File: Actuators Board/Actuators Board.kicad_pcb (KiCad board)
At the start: 2 copper layers, 96 parts, among them IC1 BD62120AEFJ-E2, J10 Conn_01x02_Male, J3 USB_C_Receptacle_USB2.0, J4 Conn_01x03_Male, J5 Conn_01x06_Male, J9 Conn_01x02_Male, Q1 MMDT2222A, Q2 SI2366DS, U1 ESP32-PICO-D4, U2 TPS54233D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

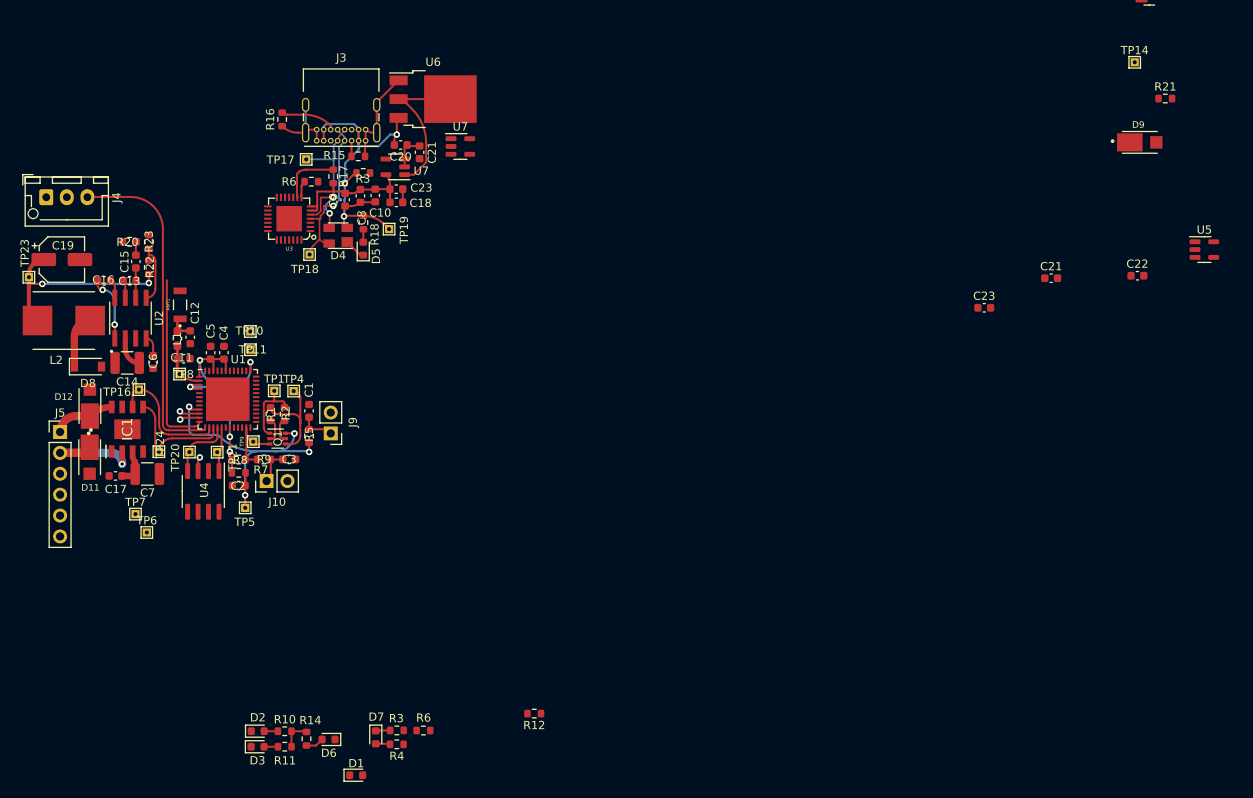
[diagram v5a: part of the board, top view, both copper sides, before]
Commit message: Swapped LDO to RT9025-25GSP & moved components closer together
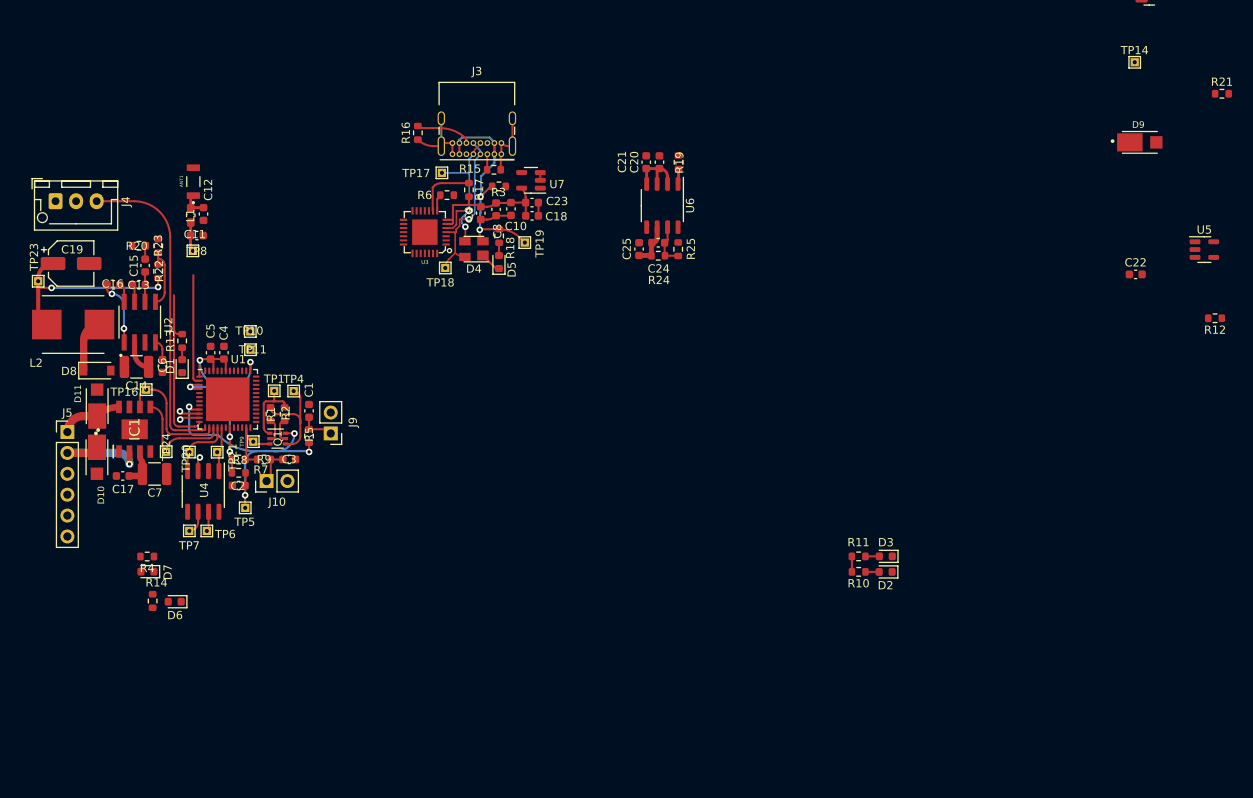
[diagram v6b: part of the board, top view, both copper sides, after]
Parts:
- removed the C21 at (260.5, 91.7)
- removed the C23 at (252.3, 95.3)
- removed the R3 at (180.9, 146.7)
- removed the R6 at (184.1, 146.7)
- removed the U7 at (188.6, 75.6)
- added C24: 0.1uF, Capacitor_SMD:C_0603_1608Metric, F.Cu at (212.7, 87.3)
- added C25: 10uF, Capacitor_SMD:C_0603_1608Metric, F.Cu at (210.4, 88.1)
- added R13: 470, Resistor_SMD:R_0603_1608Metric, F.Cu at (154.8, 99.3)
- added R19: 100k, Resistor_SMD:R_0603_1608Metric, F.Cu at (215.2, 77.6)
- added R24: 147k, Resistor_SMD:R_0603_1608Metric, F.Cu at (212.7, 88.9)
- added R25: 47k, Resistor_SMD:R_0603_1608Metric, F.Cu at (215.1, 88.1)
- C21: value 22uF -> 1uF
- U6: value AZ1084-3.3 -> RT9025-25GSP; footprint Package_TO_SOT_SMD:TO-252-3_TabPin2 -> Package_SO:SOP-8_3.9x4.9mm_P1.27mm
- moved R12 95.7 mm to (280.4, 96.5)
- moved D3 79.8 mm to (240.4, 125.5), turned to 180 degrees
- moved D2 78.8 mm to (240.3, 127.4), turned to 180 degrees
- moved R11 73.5 mm to (237.1, 125.5), turned to 0 degrees
- moved R10 72.5 mm to (237.1, 127.4), turned to 0 degrees
- moved D1 54.1 mm to (154.8, 102.4), turned to 90 degrees
- moved R4 38.0 mm to (150.5, 125.5)
- moved D7 34.3 mm to (150.6, 127.3), turned to 180 degrees
- moved C20 31.5 mm to (212.8, 77.5), turned to -90 degrees
- moved U6 30.7 mm to (213.2, 82.8), turned to -90 degrees
- moved C21 27.6 mm to (211.2, 77.5)
- moved D6 25.1 mm to (153.9, 131.0)
- moved R14 25.1 mm to (151.2, 130.9)
- moved C9 16.6 mm to (191.1, 83.8)
- moved D4 16.6 mm to (190.3, 88.1)
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- renumbered D11 to D10, D12 to D11
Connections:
- C21 pad 2: (no net) -> VBUS
- D1 pad 2: /SolEN -> Net-(D1-Pad2)
- R3 pad 2: (no net) -> Net-(R3-Pad2)
- U6 pad 1: GND -> Net-(R19-Pad1)
- U6 pad 2: Net-(C21-Pad2) -> VBUS
- U7 pad 1: Net-(C21-Pad2) -> Net-(U7-Pad1)
- U7 pad 4: (no net) -> unconnected-(U7-Pad4)
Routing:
- net Net-(C21-Pad2): track 18.6 -> 0.00 mm
- net /LNA_IN: track 6.27 -> 17.1 mm
- net GND: track 38.0 -> 29.2 mm
- net Net-(U7-Pad1): track 0.00 -> 5.39 mm
- net Net-(C24-Pad1): track 0.00 -> 5.32 mm
- net /CAN_LOW: track 0.00 -> 2.89 mm
- net /CAN_HIGH: track 0.00 -> 2.44 mm
- net Net-(D6-Pad2): track 2.20 -> 0.00 mm
- net Net-(R19-Pad1): track 0.00 -> 1.85 mm
- net /ServoPWM: track 40.7 -> 38.9 mm
- net Net-(D7-Pad2): track 1.76 -> 0.00 mm
- net +3V3: track 61.1 -> 59.3 mm
- net VBUS: track 38.2 -> 39.8 mm, vias 3 -> 2
- net Net-(D1-Pad2): track 0.00 -> 1.46 mm
- net /HBridgeDIR1: track 15.0 -> 14.1 mm
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
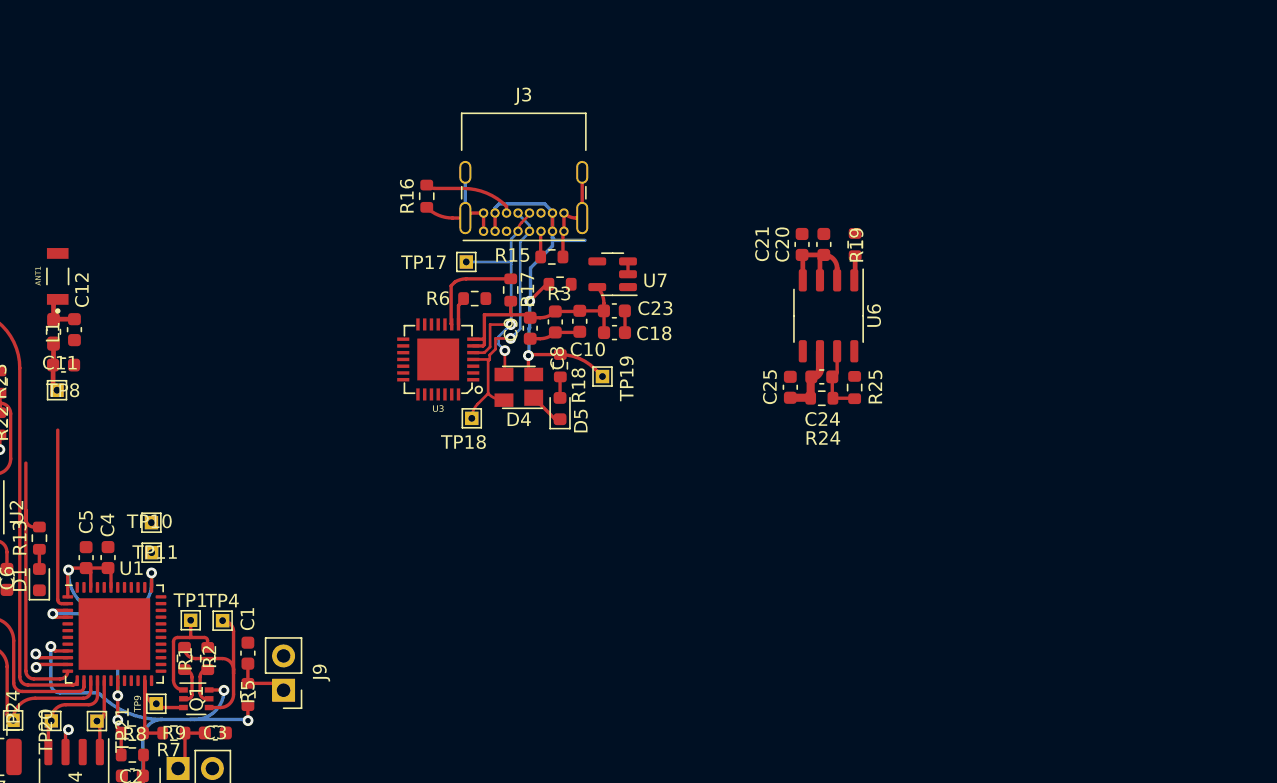
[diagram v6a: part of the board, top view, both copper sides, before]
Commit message: condensed usb layout
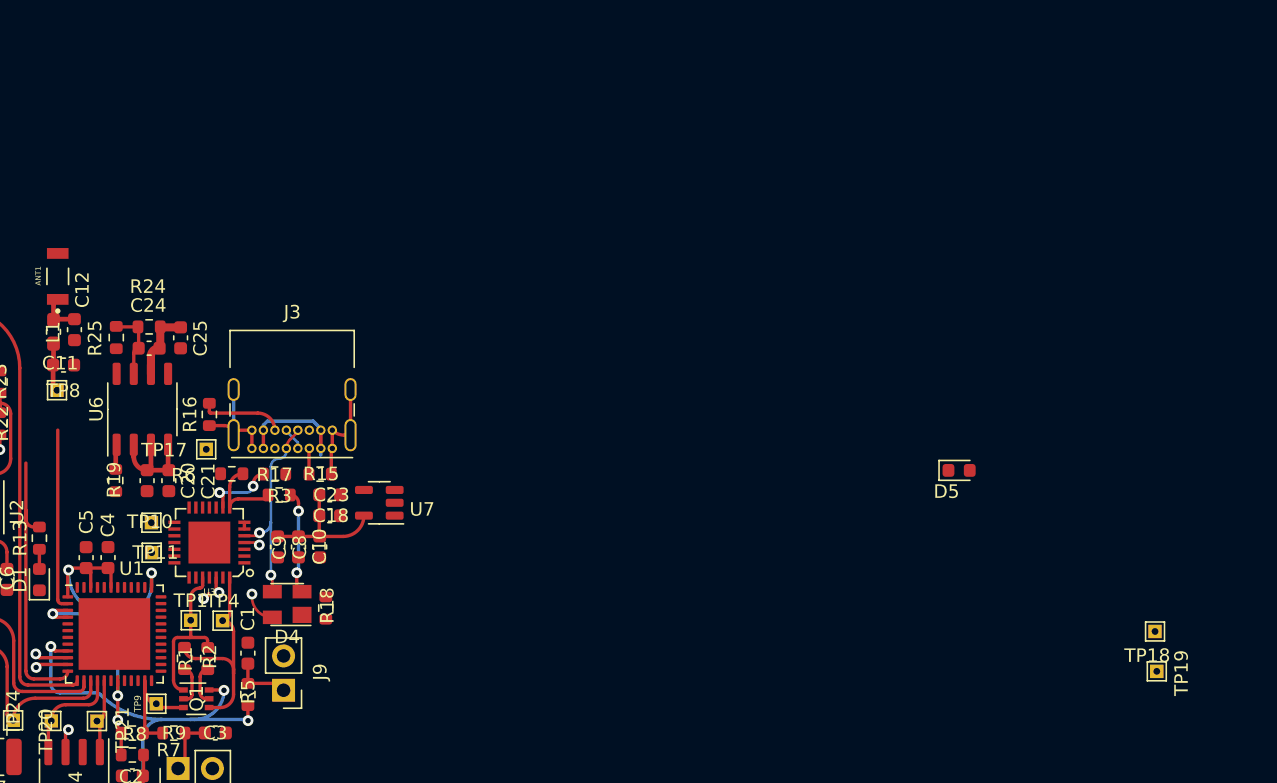
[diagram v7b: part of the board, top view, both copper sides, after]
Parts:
- moved R19 57.4 mm to (160.4, 95.0), turned to -90 degrees
- moved R25 54.8 mm to (160.5, 84.4), turned to -90 degrees
- moved C20 53.0 mm to (162.8, 95.0), turned to 90 degrees
- moved TP18 53.0 mm to (237.3, 106.2)
- moved U6 51.2 mm to (162.4, 89.8), turned to 90 degrees
- moved R24 50.1 mm to (162.9, 83.7), turned to 180 degrees
- moved C21 50.0 mm to (164.4, 95.0), turned to 90 degrees
- moved C24 49.8 mm to (162.9, 85.2), turned to 0 degrees
- moved TP19 46.5 mm to (237.5, 109.1)
- moved C25 45.3 mm to (165.2, 84.5), turned to 90 degrees
- moved D5 29.9 mm to (222.8, 94.3), turned to 0 degrees
- moved R3 26.0 mm to (172.5, 96.1), turned to 180 degrees
- moved C10 25.5 mm to (175.5, 99.9)
- moved C8 25.3 mm to (174.0, 99.9)
- moved C23 25.1 mm to (176.3, 96.1)
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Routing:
- net /USB -> UART/Data+: track 20.4 -> 5.50 mm
- net VBUS: track 39.8 -> 25.9 mm
- net GND: track 29.2 -> 19.3 mm
- net +3V3: track 59.3 -> 52.5 mm
- net /USB -> UART/Data-: track 21.0 -> 15.5 mm, vias 2 -> 1
- net Net-(R3-Pad2): track 1.73 -> 6.46 mm
- net /RTS: track 8.59 -> 12.2 mm
- net /DTR: track 13.0 -> 16.5 mm
- net Net-(R17-Pad2): track 7.44 -> 5.58 mm, vias 0 -> 2
- net Net-(D5-Pad2): track 1.63 -> 0.00 mm
- net /TXD: track 0.00 -> 1.22 mm
- net Net-(J3-PadB5): track 7.13 -> 6.20 mm
- net /RXD: track 0.00 -> 0.58 mm
- net (no net): vias 0 -> 4

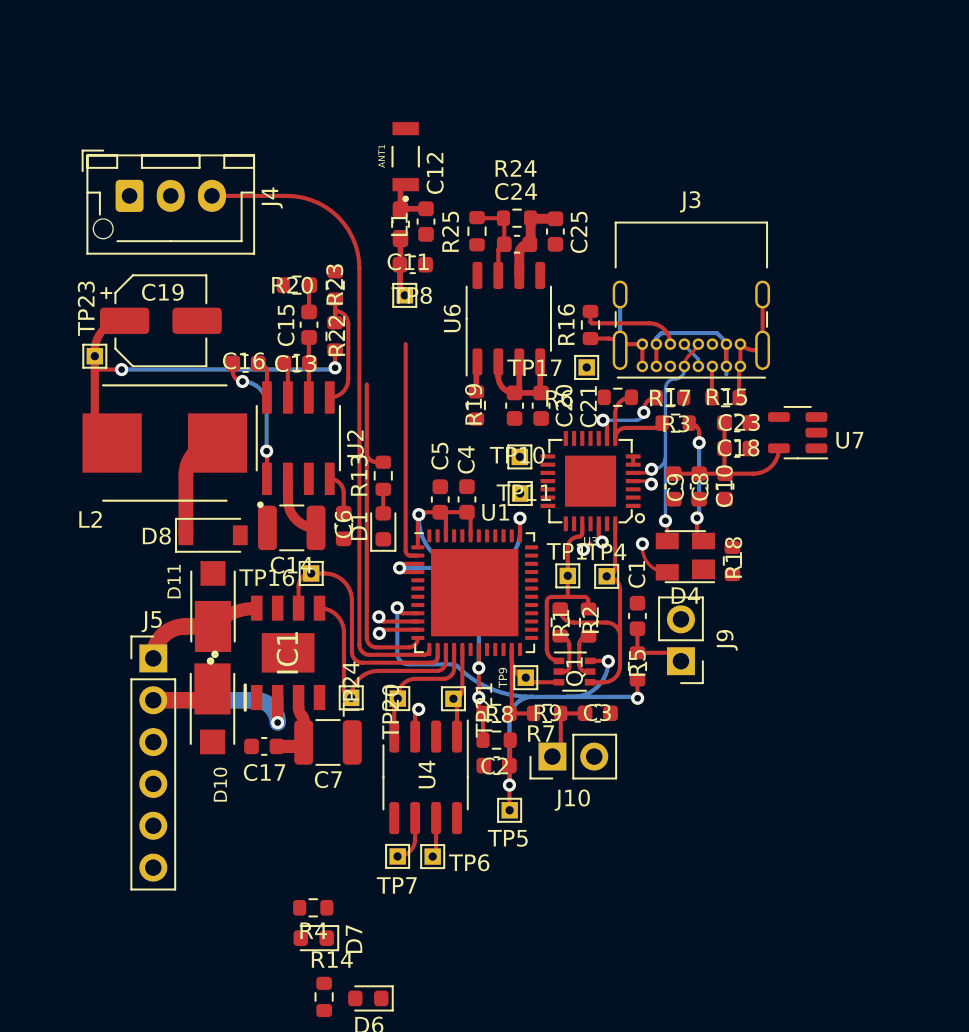
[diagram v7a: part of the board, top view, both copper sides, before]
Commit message: Rearranged buck converter to allow for datasheet ground areas
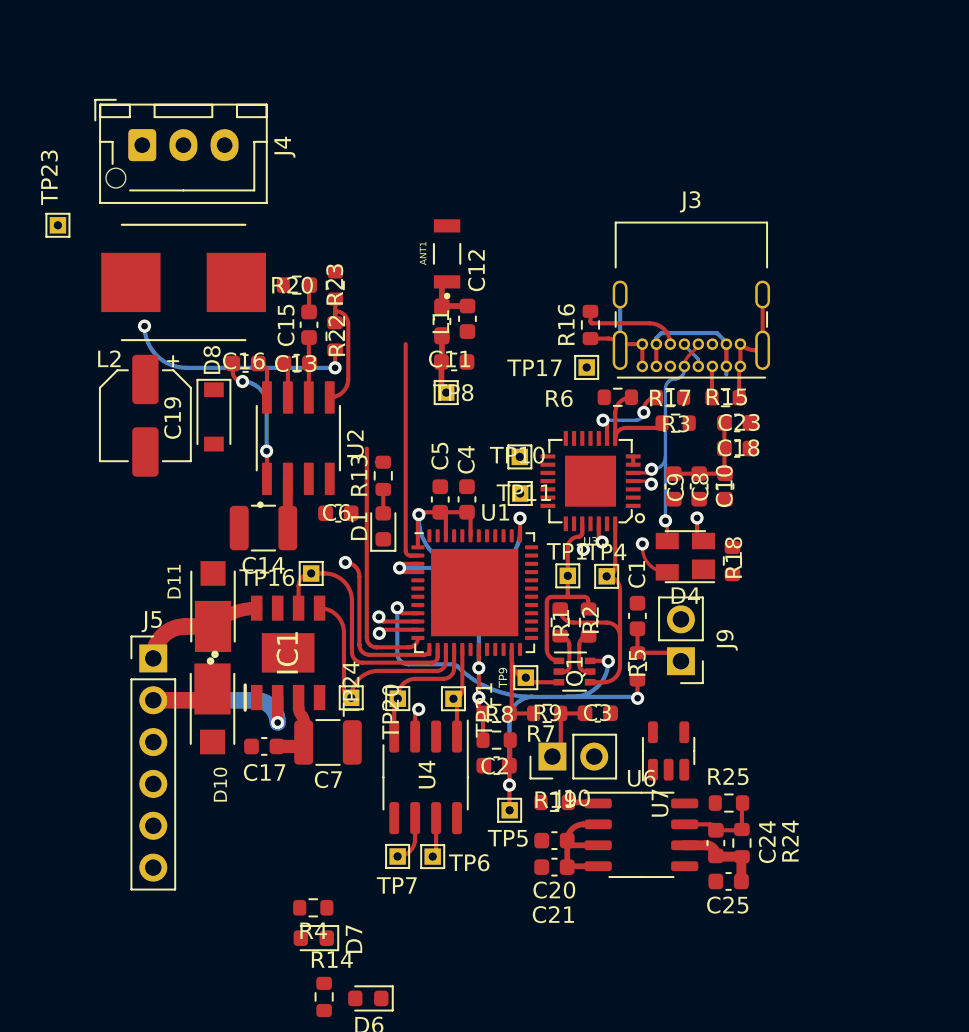
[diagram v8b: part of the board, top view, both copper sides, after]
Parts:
- moved C25 40.8 mm to (175.8, 123.9), turned to 0 degrees
- moved R24 40.3 mm to (176.6, 121.6), turned to 90 degrees
- moved C24 38.3 mm to (175.0, 121.6), turned to -90 degrees
- moved R25 37.9 mm to (175.8, 119.2), turned to 180 degrees
- moved U6 32.3 mm to (170.5, 121.1), turned to 0 degrees
- moved C21 28.0 mm to (165.2, 123.0), turned to 0 degrees
- moved C20 26.5 mm to (165.2, 121.4), turned to 0 degrees
- moved R19 24.6 mm to (165.2, 119.1), turned to 180 degrees
- moved U7 20.9 mm to (172.1, 116.0), turned to 90 degrees
- moved L2 9.81 mm to (142.7, 87.5)
- moved TP23 8.26 mm to (135.0, 84.1)
- moved D8 7.19 mm to (144.5, 95.7), turned to -90 degrees
- moved TP8 6.41 mm to (158.6, 94.2)
- moved C11 6.41 mm to (159.1, 92.4)
- moved L1 6.41 mm to (158.3, 89.9)
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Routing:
- net /ServoPWM: track 38.9 -> 10.2 mm, vias 0 -> 1
- net +6V: track 24.7 -> 14.2 mm
- net Net-(C16-Pad2): track 10.3 -> 2.34 mm
- net VBUS: track 25.9 -> 19.8 mm, vias 2 -> 1
- net /SolEN: track 21.1 -> 15.6 mm
- net +3V3: track 52.5 -> 48.4 mm
- net Net-(C6-Pad1): track 2.54 -> 0.00 mm
- net +24V: track 8.92 -> 8.02 mm
- net /RXD: track 0.58 -> 0.00 mm
